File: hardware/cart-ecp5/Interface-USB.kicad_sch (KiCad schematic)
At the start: 42 parts, among them J5 USB_C_USB2.0, U10 93C46BT-I_OT, U11 FT2232HQ, U3 USBLC6-2SC6, X2 SiT2001B

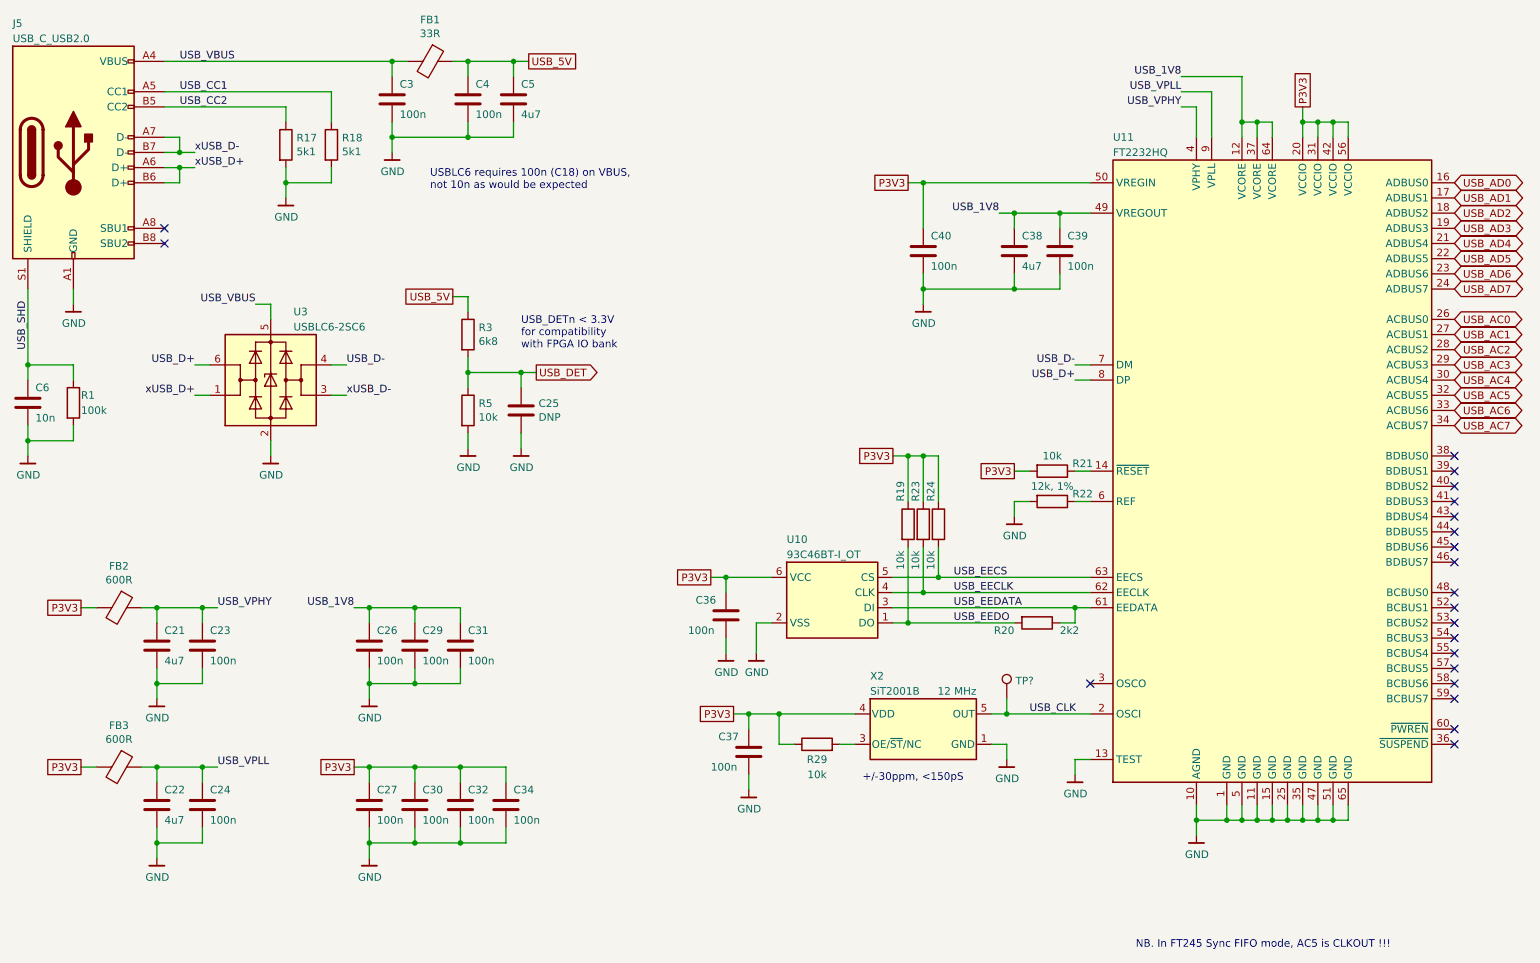
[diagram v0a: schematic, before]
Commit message: hardware: Substitute library symbol for USB-C connector
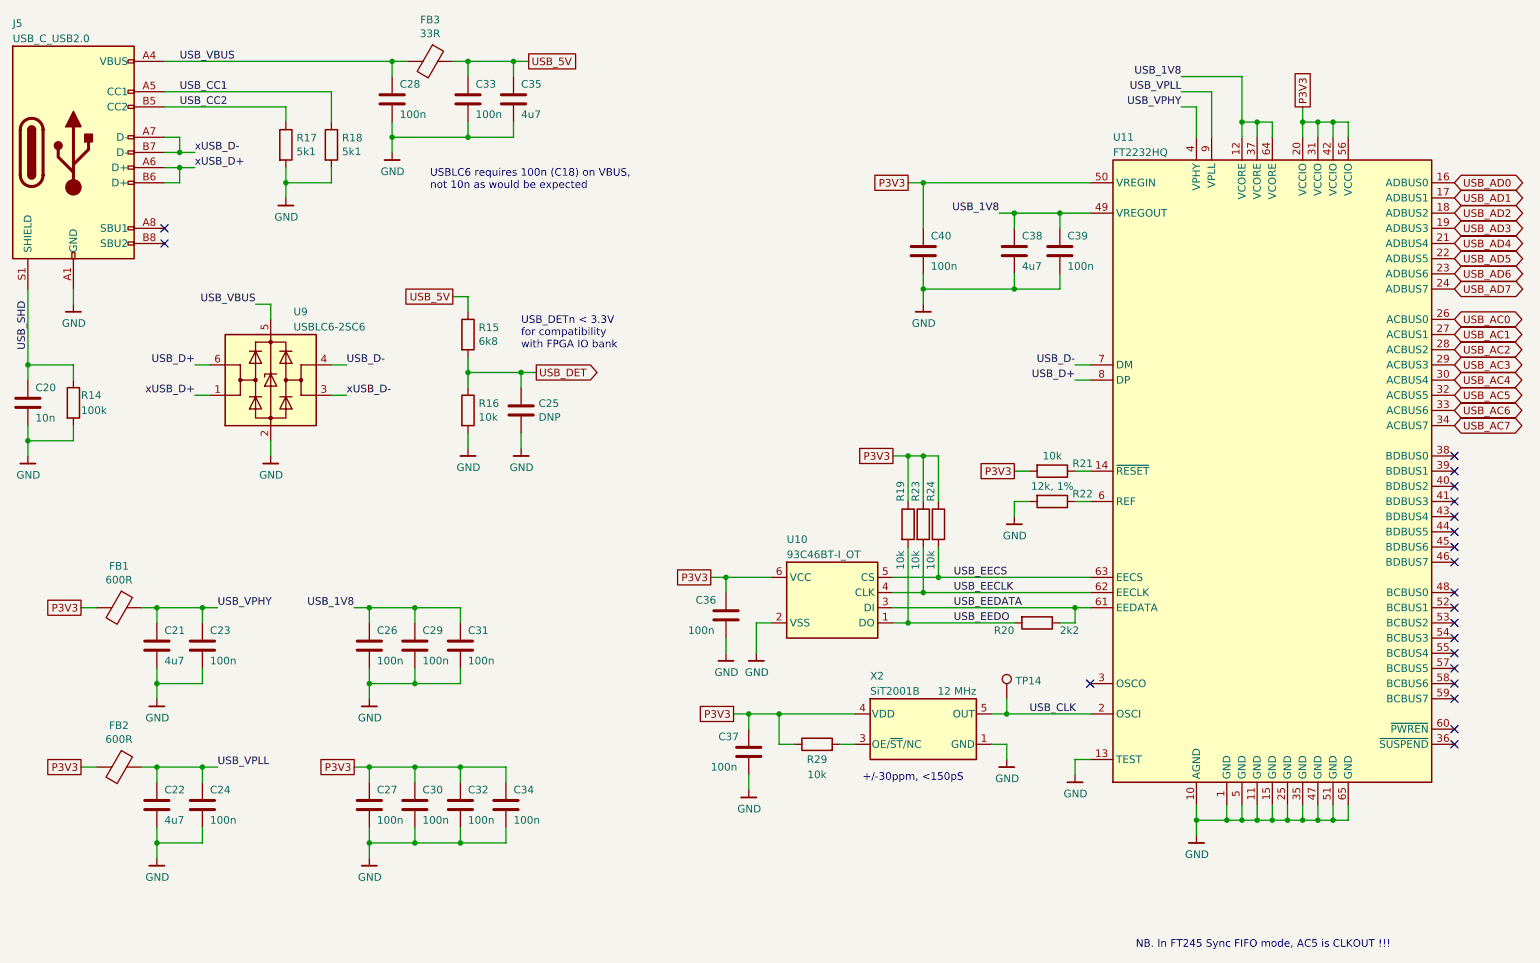
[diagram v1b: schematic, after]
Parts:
- J5: symbol cart-ecp5-rescue:USB_C_Receptacle_USB2.0-Connector -> Connector:USB_C_Receptacle_USB2.0_16P
- gave numbers to parts that had none: 1
- renumbered C6 to C20, C3 to C28, C4 to C33, C5 to C35, FB2 to FB1, FB3 to FB2, FB1 to FB3, R1 to R14, R3 to R15, R5 to R16, U3 to U9

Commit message: hardware: Substitute library symbol for ferrite bead
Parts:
- FB1, FB2, FB3: symbol cart-ecp5-rescue:Ferrite_Bead-Device -> Device:FerriteBead
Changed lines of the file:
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@@
 	)
 	(symbol
-		(lib_id "cart-ecp5-rescue:Ferrite_Bead-Device")
+		(lib_id "Device:FerriteBead")
 		(at 157.48 73.66 270)
 		(unit 1)
@@
 	)
 	(symbol
-		(lib_id "cart-ecp5-rescue:Ferrite_Bead-Device")
+		(lib_id "Device:FerriteBead")
 		(at 105.41 165.1 270)
 		(unit 1)
@@
 	)
 	(symbol
-		(lib_id "cart-ecp5-rescue:Ferrite_Bead-Device")
+		(lib_id "Device:FerriteBead")
 		(at 105.41 191.77 270)
 		(unit 1)

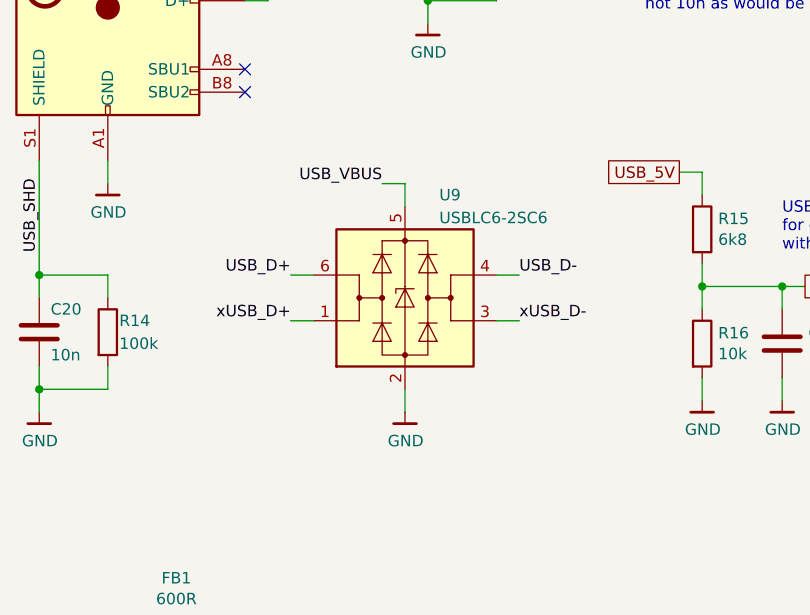
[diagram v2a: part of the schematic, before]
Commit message: hardware: Substitute library symbol for USBLC6
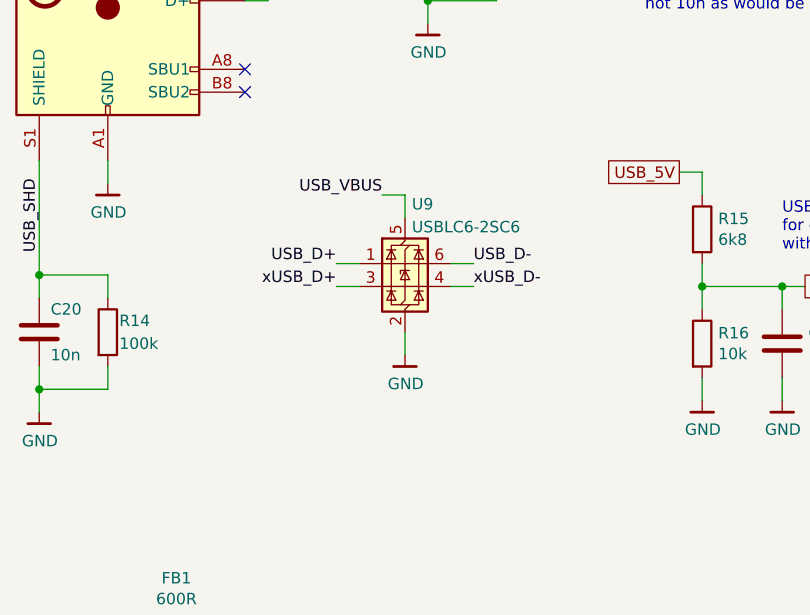
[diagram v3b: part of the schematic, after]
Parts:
- U9: symbol cart-ecp5-rescue:USBLC6-2SC6-Power_Protection -> Power_Protection:USBLC6-2SC6
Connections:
- net USB_D+: now also U9.1 (I/O1); no longer U9.6 (I/O1)
- net USB_D-: now also U9.6 (I/O1); no longer U9.4 (I/O2)
- net xUSB_D+: now also U9.3 (I/O2); no longer U9.1 (I/O1)
- net xUSB_D-: now also U9.4 (I/O2); no longer U9.3 (I/O2)
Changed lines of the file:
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@@
 	(wire
 		(pts
-			(xy 128.27 114.3) (xy 130.81 114.3)
+			(xy 128.27 115.57) (xy 130.81 115.57)
 		)
 		(stroke
@@
 	(wire
 		(pts
-			(xy 130.81 114.3) (xy 130.81 116.84)
+			(xy 130.81 115.57) (xy 130.81 118.11)
 		)
 		(stroke
@@
 	(wire
 		(pts
-			(xy 140.97 124.46) (xy 143.51 124.46)
+			(xy 135.89 123.19) (xy 138.43 123.19)
 		)
 		(stroke
@@
 	(wire
 		(pts
-			(xy 120.65 129.54) (xy 118.11 129.54)
+			(xy 125.73 125.73) (xy 123.19 125.73)
 		)
 		(stroke
@@
 	(wire
 		(pts
-			(xy 120.65 124.46) (xy 118.11 124.46)
+			(xy 125.73 123.19) (xy 123.19 123.19)
 		)
 		(stroke
@@
 	(wire
 		(pts
-			(xy 143.51 129.54) (xy 140.97 129.54)
+			(xy 138.43 125.73) (xy 135.89 125.73)
 		)
 		(stroke
@@
 	(wire
 		(pts
-			(xy 130.81 137.16) (xy 130.81 139.7)
+			(xy 130.81 130.81) (xy 130.81 133.35)
 		)
 		(stroke
@@
 	)
 	(label "USB_D-"
-		(at 143.51 124.46 0)
+		(at 138.43 123.19 0)
 		(fields_autoplaced yes)
 		(effects
@@
 	)
 	(label "USB_VBUS"
-		(at 128.27 114.3 180)
+		(at 128.27 115.57 180)
 		(fields_autoplaced yes)
 		(effects
@@
 	)
 	(label "USB_D+"
-		(at 118.11 124.46 180)
+		(at 123.19 123.19 180)
 		(fields_autoplaced yes)
 		(effects
@@
 	)
 	(label "xUSB_D+"
-		(at 118.11 129.54 180)
+		(at 123.19 125.73 180)
 		(fields_autoplaced yes)
 		(effects
@@
 	)
 	(label "xUSB_D-"
-		(at 143.51 129.54 0)
+		(at 138.43 125.73 0)
 		(fields_autoplaced yes)
 		(effects
@@
 	)
 	(symbol
-		(lib_id "cart-ecp5-rescue:USBLC6-2SC6-Power_Protection")
-		(at 130.81 127 0)
+		(lib_id "Power_Protection:USBLC6-2SC6")
+		(at 130.81 123.19 0)
 		(unit 1)
 		(exclude_from_sim no)
@@
 		(dnp no)
 		(property "Reference" "U9"
-			(at 134.62 115.57 0)
+			(at 131.572 116.586 0)
 			(effects
 				(font
@@
 		)
 		(property "Value" "USBLC6-2SC6"
-			(at 134.62 118.11 0)
+			(at 131.572 119.126 0)
 			(effects
 				(font
@@
 		)
 		(property "Footprint" "Package_TO_SOT_SMD:SOT-23-6"
-			(at 111.76 116.84 0)
+			(at 111.76 113.03 0)
 			(effects
 				(font
@@
 		)
 		(property "Datasheet" "http://www2.st.com/resource/en/datasheet/CD00050750.pdf"
-			(at 135.89 118.11 0)
+			(at 135.89 114.3 0)
 			(effects
 				(font
@@
 		)
 		(property "Description" ""
-			(at 130.81 127 0)
+			(at 130.81 123.19 0)
 			(effects
 				(font
@@
 		)
 		(property "MFR" "ST"
-			(at 130.81 127 0)
+			(at 130.81 123.19 0)
 			(effects
 				(font
@@
 		)
 		(property "MPN" "USBLC6-2SC6"
-			(at 130.81 127 0)
+			(at 130.81 123.19 0)
 			(effects
 				(font
@@
 	(symbol
 		(lib_id "ng_power:GND")
-		(at 130.81 139.7 0)
+		(at 130.81 133.35 0)
 		(unit 1)
 		(exclude_from_sim no)
@@
 		(dnp no)
 		(property "Reference" "#PWR040"
-			(at 130.81 146.05 0)
+			(at 130.81 139.7 0)
 			(effects
 				(font
@@
 		)
 		(property "Value" "GND"
-			(at 130.8862 142.9004 0)
+			(at 130.8862 136.5504 0)
 			(effects
 				(font
@@
 		)
 		(property "Footprint" ""
-			(at 128.27 148.59 0)
+			(at 128.27 142.24 0)
 			(effects
 				(font
@@
 		)
 		(property "Datasheet" ""
-			(at 130.81 139.7 0)
+			(at 130.81 133.35 0)
 			(effects
 				(font
@@
 		)
 		(property "Description" ""
-			(at 130.81 139.7 0)
+			(at 130.81 133.35 0)
 			(effects
 				(font

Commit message: hardware: Fix swapped USB nets on schematic
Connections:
- net USB_D+: now also U9.6 (I/O1); no longer U9.1 (I/O1)
- net USB_D-: now also U9.4 (I/O2); no longer U9.6 (I/O1)
- net xUSB_D+: now also U9.1 (I/O1); no longer U9.3 (I/O2)
- net xUSB_D-: now also U9.3 (I/O2); no longer U9.4 (I/O2)
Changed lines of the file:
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@@
 	)
 	(label "USB_D-"
-		(at 138.43 123.19 0)
+		(at 138.43 125.73 0)
 		(fields_autoplaced yes)
 		(effects
@@
 	)
 	(label "USB_D+"
-		(at 123.19 123.19 180)
+		(at 138.43 123.19 0)
 		(fields_autoplaced yes)
 		(effects
@@
 				(size 1.27 1.27)
 			)
-			(justify right bottom)
+			(justify left bottom)
 		)
 	)
@@
 	)
 	(label "xUSB_D+"
+		(at 123.19 123.19 180)
+		(fields_autoplaced yes)
+		(effects
+			(font
+				(size 1.27 1.27)
+			)
+			(justify right bottom)
+		)
+	)
+	(label "xUSB_D-"
 		(at 123.19 125.73 180)
 		(fields_autoplaced yes)
@@
 		)
 	)
-	(label "xUSB_D-"
-		(at 138.43 125.73 0)
-		(fields_autoplaced yes)
-		(effects
-			(font
-				(size 1.27 1.27)
-			)
-			(justify left bottom)
-		)
-	)
